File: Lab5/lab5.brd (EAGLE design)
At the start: 130 x 130 mm, 54 parts, among them J1 ISP, Q1 SI2302CDS, Q2 SI2302CDS, Q3 SI2302CDS, Q4 SI2302CDS, U1 ATMEGA128RFA1, Y1 16MHz

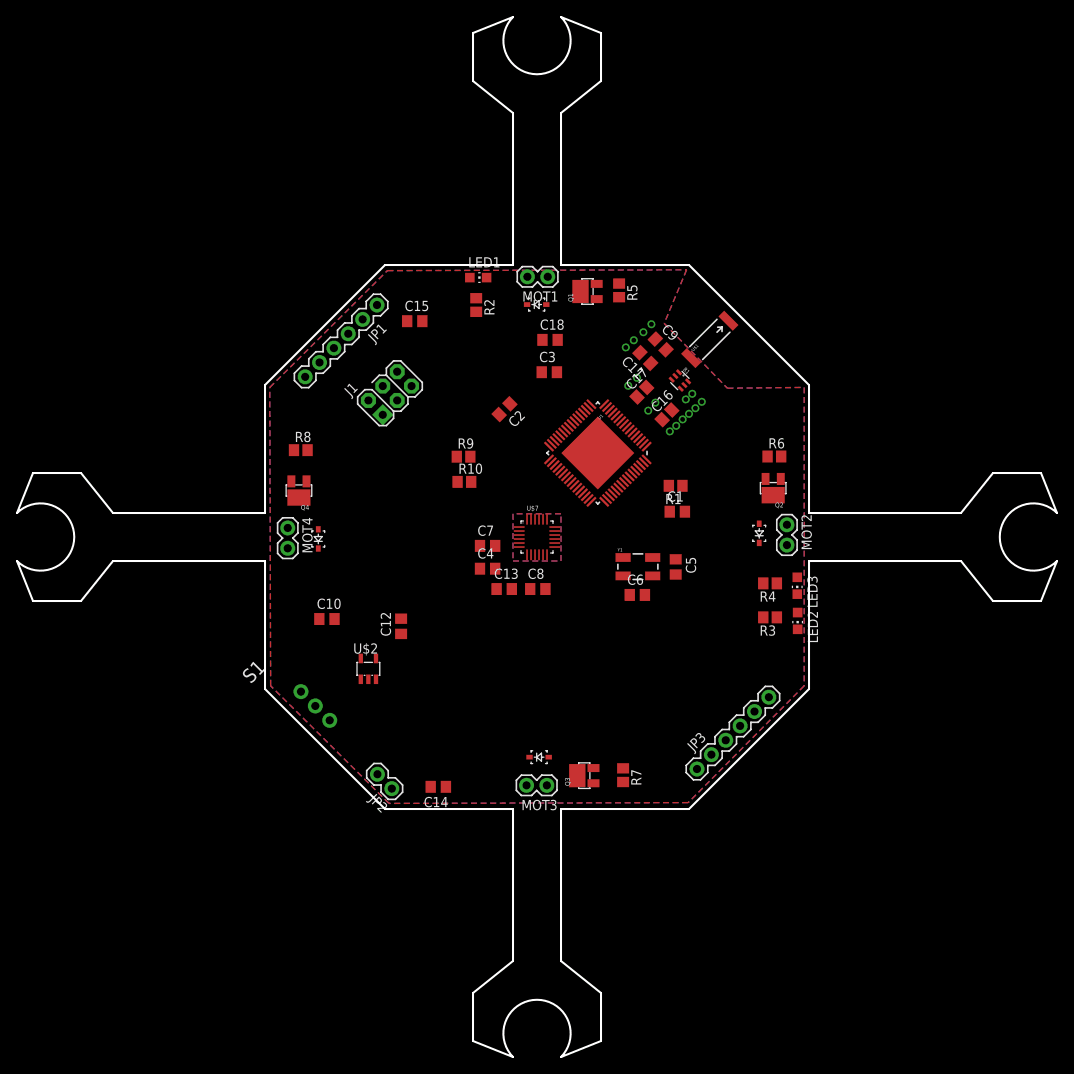
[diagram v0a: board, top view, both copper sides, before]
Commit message: working on making the board smaller
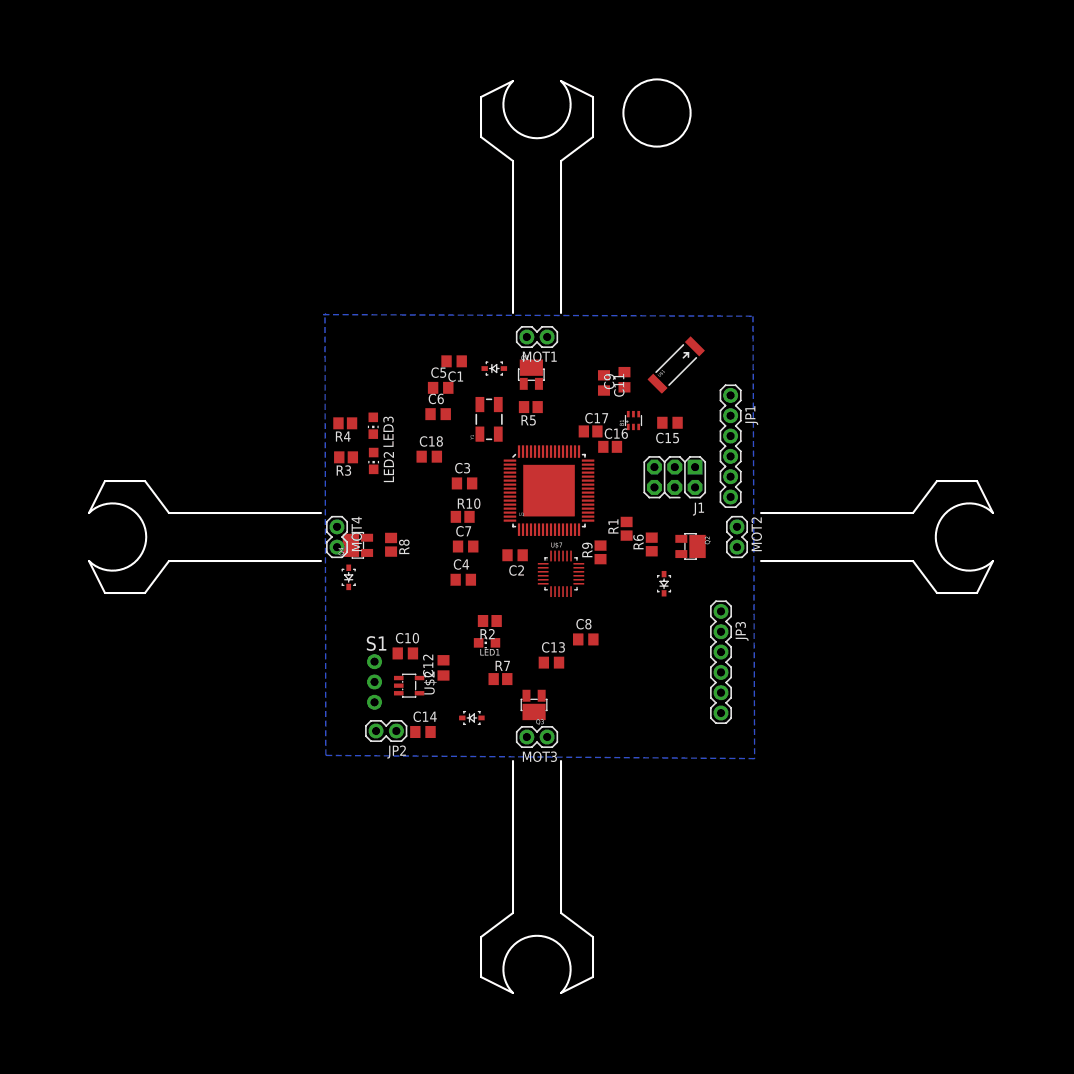
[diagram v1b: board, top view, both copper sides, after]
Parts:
- moved R4 56.7 mm to (-24.0, 14.2)
- moved LED2 56.6 mm to (-20.4, 9.51)
- moved LED3 56.6 mm to (-20.5, 13.9)
- moved R3 56.6 mm to (-23.9, 9.96)
- moved LED1 45.7 mm to (-6.25, -13.2), turned to 90 degrees
- moved JP1 45.6 mm to (24.2, 17.7), turned to 270 degrees
- moved R2 39.5 mm to (-5.90, -10.5), turned to 180 degrees
- moved J1 37.1 mm to (17.2, 7.47), turned to 180 degrees
- moved C5 36.9 mm to (-12.0, 18.6), turned to 0 degrees
- moved C15 34.3 mm to (16.6, 14.3), turned to 180 degrees
- moved C1 33.6 mm to (-10.4, 22.0), turned to 180 degrees
- moved C6 33.6 mm to (-12.4, 15.4)
- moved Y1 26.2 mm to (-5.99, 14.7), turned to 90 degrees
- moved C18 21.0 mm to (-13.5, 10.0)
- moved R9 20.9 mm to (7.94, -1.92), turned to 90 degrees
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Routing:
- removed copper zone on layer 1, net GND
- removed copper zone on layer 1, net N$1
- removed copper zone on layer 16, net N$1
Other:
- board size 130 x 130 mm -> 113 x 114.2 mm

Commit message: finisehd board. but need to add names
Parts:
- added U$3, U$4: (no value), lab5_comps:BEE_LOGO
- moved R4 39.6 mm to (15.6, 13.8), turned to 270 degrees
- moved R3 36.7 mm to (12.7, 13.7), turned to 270 degrees
- moved LED3 36.3 mm to (15.6, 18.3), turned to 0 degrees
- moved U$1 35.8 mm to (-18.2, 18.2), turned to 135 degrees
- moved LED2 34.2 mm to (12.6, 18.1), turned to 0 degrees
- moved C18 30.3 mm to (9.04, -10.3), turned to 270 degrees
- moved C9 28.5 mm to (-16.7, 12.4), turned to 225 degrees
- moved B1 25.3 mm to (-13.2, 13.6), turned to 315 degrees
- moved C11 24.9 mm to (-15.1, 10.8), turned to 45 degrees
- moved C5 21.2 mm to (9.16, 18.0), turned to 90 degrees
- moved C6 18.9 mm to (6.34, 17.9), turned to 90 degrees
- moved JP3 18.8 mm to (7.00, -19.2), turned to 0 degrees
- moved J1 18.5 mm to (14.7, -10.9), turned to 270 degrees
- moved C17 18.2 mm to (-11.2, 10.1), turned to 135 degrees
- moved C16 18.2 mm to (-8.97, 12.5), turned to 135 degrees
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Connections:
- net GND: no longer U1.65
- net PB5: now also Q2.G, R6.2; no longer Q1.G, R5.2
- net PE5: now also Q1.G, R5.2; no longer Q2.G, R6.2
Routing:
- net VBAT: track 0.00 -> 104.7 mm, vias 0 -> 1
- net 3V: track 0.00 -> 92.3 mm, vias 0 -> 6
- net GND: track 0.00 -> 43.7 mm, vias 0 -> 35
- net RESET: track 0.00 -> 41.0 mm, vias 0 -> 2
- net PE3: track 0.00 -> 27.8 mm, vias 0 -> 2
- net TX1: track 0.00 -> 24.7 mm, vias 0 -> 2
- net PE4: track 0.00 -> 24.5 mm, vias 0 -> 2
- net MOSI: track 0.00 -> 24.0 mm, vias 0 -> 1
- net RX1: track 0.00 -> 23.9 mm, vias 0 -> 2
- net N$5: track 0.00 -> 19.9 mm, vias 0 -> 2
- net SCK: track 0.00 -> 16.8 mm
- net MISO: track 0.00 -> 16.4 mm
- net RX0: track 0.00 -> 16.1 mm, vias 0 -> 2
- net PB5: track 0.00 -> 15.7 mm, vias 0 -> 2
- net TX0: track 0.00 -> 15.5 mm, vias 0 -> 2
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- added copper zone on layer 1, net GND
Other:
- board size 113 x 114.2 mm -> 104 x 104 mm

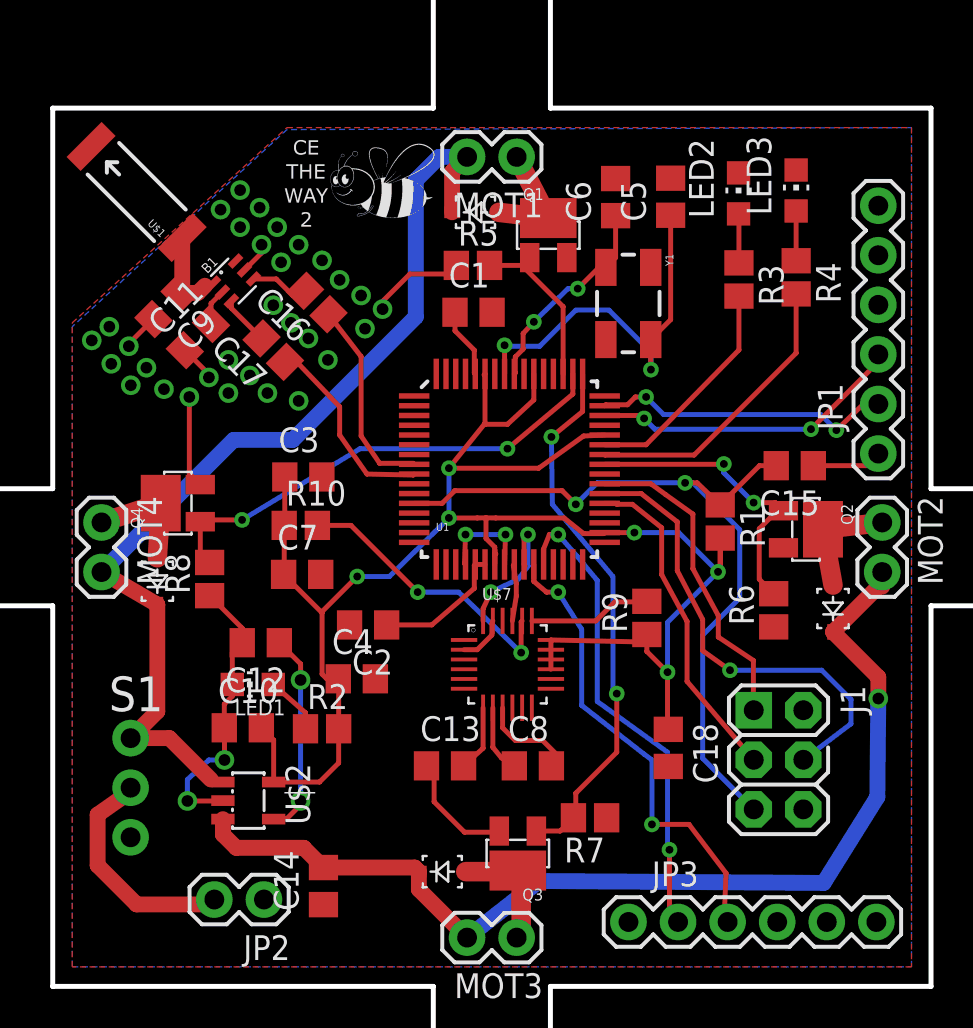
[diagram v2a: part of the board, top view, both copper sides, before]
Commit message: Update The Board Some Component Names
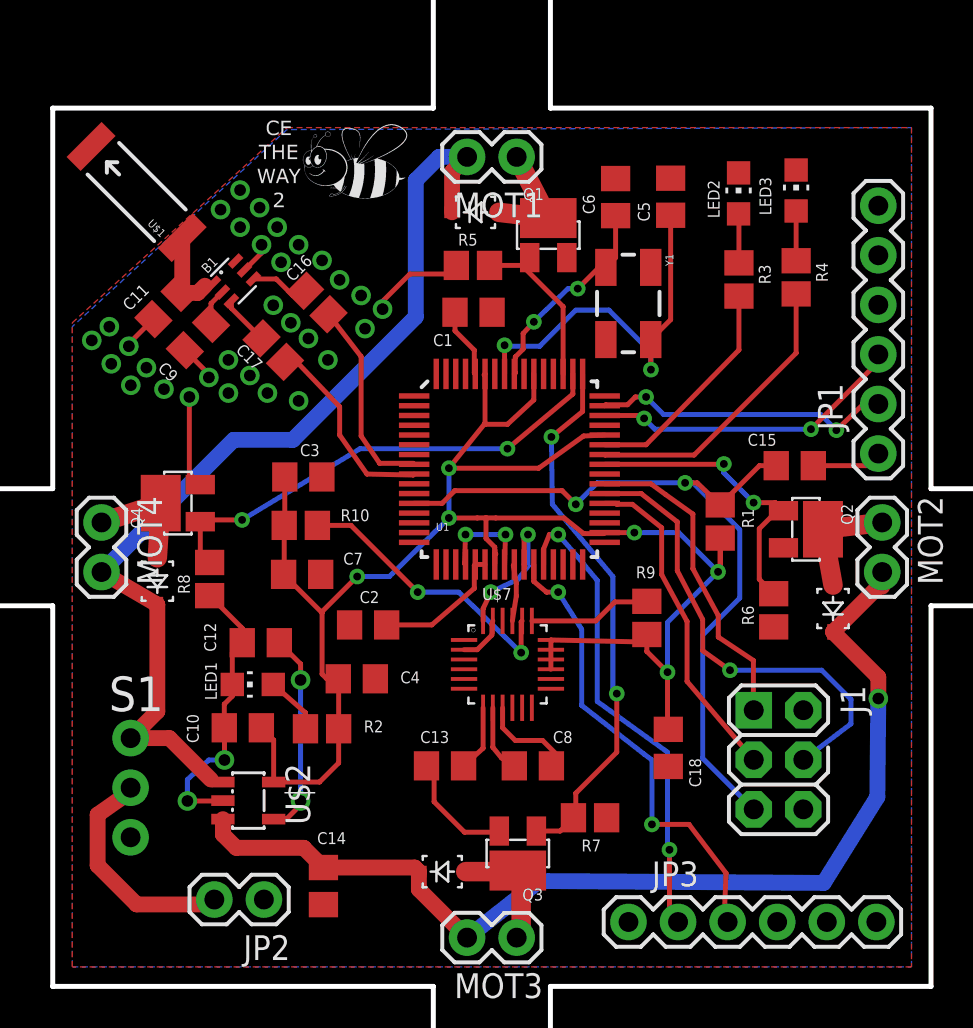
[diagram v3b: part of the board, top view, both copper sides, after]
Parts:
- moved U$3 1.72 mm to (-8.10, 19.5)

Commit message: final board design
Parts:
- moved U$3 1.04 mm to (-7.10, 19.2)
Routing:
- net GND: track 43.7 -> 33.4 mm, vias 35 -> 49
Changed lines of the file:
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@@
 <setting verticaltext="up"/>
 </settings>
-<grid distance="0.1" unitdist="mm" unit="mm" style="lines" multiple="1" display="yes" altdistance="0.025" altunitdist="inch" altunit="inch"/>
+<grid distance="0.5" unitdist="mm" unit="mm" style="lines" multiple="1" display="yes" altdistance="0.025" altunitdist="inch" altunit="inch"/>
 <layers>
 <layer number="1" name="Top" color="4" fill="1" visible="yes" active="yes"/>
@@
 <wire x1="-22.5" y1="3" x2="-22.5" y2="22.5" width="0.254" layer="20"/>
 <wire x1="-22.5" y1="-22.5" x2="-22.5" y2="-3" width="0.254" layer="20"/>
-<polygon width="0.254" layer="41">
-<vertex x="-22" y="21.9"/>
-<vertex x="-22" y="11"/>
-<vertex x="-10" y="22"/>
-<vertex x="-22" y="22"/>
-</polygon>
 <polygon width="0.254" layer="42">
 <vertex x="-22" y="22"/>
-<vertex x="-22" y="11"/>
-<vertex x="-10" y="22"/>
+<vertex x="-10.5" y="22"/>
+<vertex x="-22" y="11.5"/>
+</polygon>
+<polygon width="0.254" layer="41">
+<vertex x="-22" y="22"/>
+<vertex x="-10.5" y="22"/>
+<vertex x="-22" y="11.5"/>
 </polygon>
 </plain>
@@
 <attribute name="TOL" value="" x="-17.14" y="-1.74" size="1.778" layer="27" rot="R90" display="off"/>
 </element>
-<element name="U$3" library="lab5_comps" package="BEE_LOGO" value="" x="-8.1" y="19.5"/>
+<element name="U$3" library="lab5_comps" package="BEE_LOGO" value="" x="-7.1" y="19.2"/>
 <element name="U1" library="lab5_comps" package="QFN-64" value="ATMEGA128RFA1" x="0.9" y="4"/>
 <element name="U$4" library="lab5_comps" package="BEE_LOGO" value="" x="0.3" y="32.8" rot="R90"/>
@@
 <wire x1="-14.46" y1="-2.48" x2="-12.79" y2="-4.15" width="0.254" layer="1"/>
 <wire x1="-12.79" y1="-4.15" x2="-12.79" y2="-4.89" width="0.254" layer="1"/>
-<wire x1="-13.71" y1="-8.04" x2="-13.71" y2="-9.25" width="0.254" layer="1"/>
 <wire x1="-13.71" y1="-9.25" x2="-13.7" y2="-9.25" width="0.254" layer="1"/>
-<wire x1="-13.7" y1="-9.25" x2="-13.7" y2="-10.9" width="0.254" layer="1"/>
-<via x="-13.7" y="-10.9" extent="1-16" drill="0.6"/>
-<wire x1="-13.7" y1="-10.9" x2="-14.5" y2="-10.9" width="0.254" layer="16"/>
-<wire x1="-14.5" y1="-10.9" x2="-15.6" y2="-11.9" width="0.254" layer="16"/>
-<wire x1="-15.6" y1="-11.9" x2="-15.6" y2="-13" width="0.254" layer="16"/>
-<via x="-15.6" y="-13" extent="1-16" drill="0.6"/>
-<wire x1="-15.6" y1="-13" x2="-13.8" y2="-13" width="0.254" layer="1"/>
-<wire x1="-13.8" y1="-13" x2="-13.78" y2="-12.98" width="0.254" layer="1"/>
-<wire x1="-13.71" y1="-8.04" x2="-13.3" y2="-7.63" width="0.254" layer="1"/>
 <wire x1="-13.3" y1="-7.63" x2="-13.3" y2="-7.03" width="0.254" layer="1"/>
 <wire x1="-12.79" y1="-4.89" x2="-13.3" y2="-5.4" width="0.254" layer="1"/>
-<wire x1="-13.3" y1="-5.4" x2="-13.3" y2="-7.03" width="0.254" layer="1"/>
 <wire x1="-3.35" y1="-11.2" x2="-2.96" y2="-11.2" width="0.254" layer="1"/>
 <wire x1="-15.5" y1="7.7" x2="-15.5" y2="3.77" width="0.254" layer="1"/>
@@
 <wire x1="-1.4" y1="-14.6" x2="0.32" y2="-14.6" width="0.254" layer="1"/>
 <wire x1="0.32" y1="-14.6" x2="0.38" y2="-14.54" width="0.254" layer="1"/>
+<via x="-7.2" y="-12.5" extent="1-16" drill="0.4"/>
+<via x="-6.2" y="-14" extent="1-16" drill="0.4"/>
+<via x="-4.4" y="-14.1" extent="1-16" drill="0.4"/>
+<via x="-2.5" y="-14.1" extent="1-16" drill="0.4"/>
+<via x="-5.8" y="-11.2" extent="1-16" drill="0.4"/>
+<via x="-4.6" y="-9.2" extent="1-16" drill="0.4"/>
+<via x="-20.4" y="7" extent="1-16" drill="0.4"/>
+<via x="-19.6" y="4.7" extent="1-16" drill="0.4"/>
+<via x="-17.1" y="5.2" extent="1-16" drill="0.4"/>
+<via x="-18.3" y="6.5" extent="1-16" drill="0.4"/>
+<via x="-6.1" y="14.7" extent="1-16" drill="0.4"/>
+<via x="-7.4" y="15.8" extent="1-16" drill="0.4"/>
+<via x="10.5" y="10.6" extent="1-16" drill="0.4"/>
+<via x="10.6" y="13.3" extent="1-16" drill="0.4"/>
+<via x="-5.9" y="-19.9" extent="1-16" drill="0.4"/>
+<via x="-17.5" y="-20.5" extent="1-16" drill="0.4"/>
 <wire x1="5.781" y1="6.25" x2="5.781" y2="1.25" width="0" layer="19" extent="1-1"/>
 <wire x1="1.65" y1="8.881" x2="5.781" y2="6.25" width="0" layer="19" extent="1-1"/>
@@
 </signal>
 </signals>
+<errors>
+</errors>
 </board>
 </drawing>

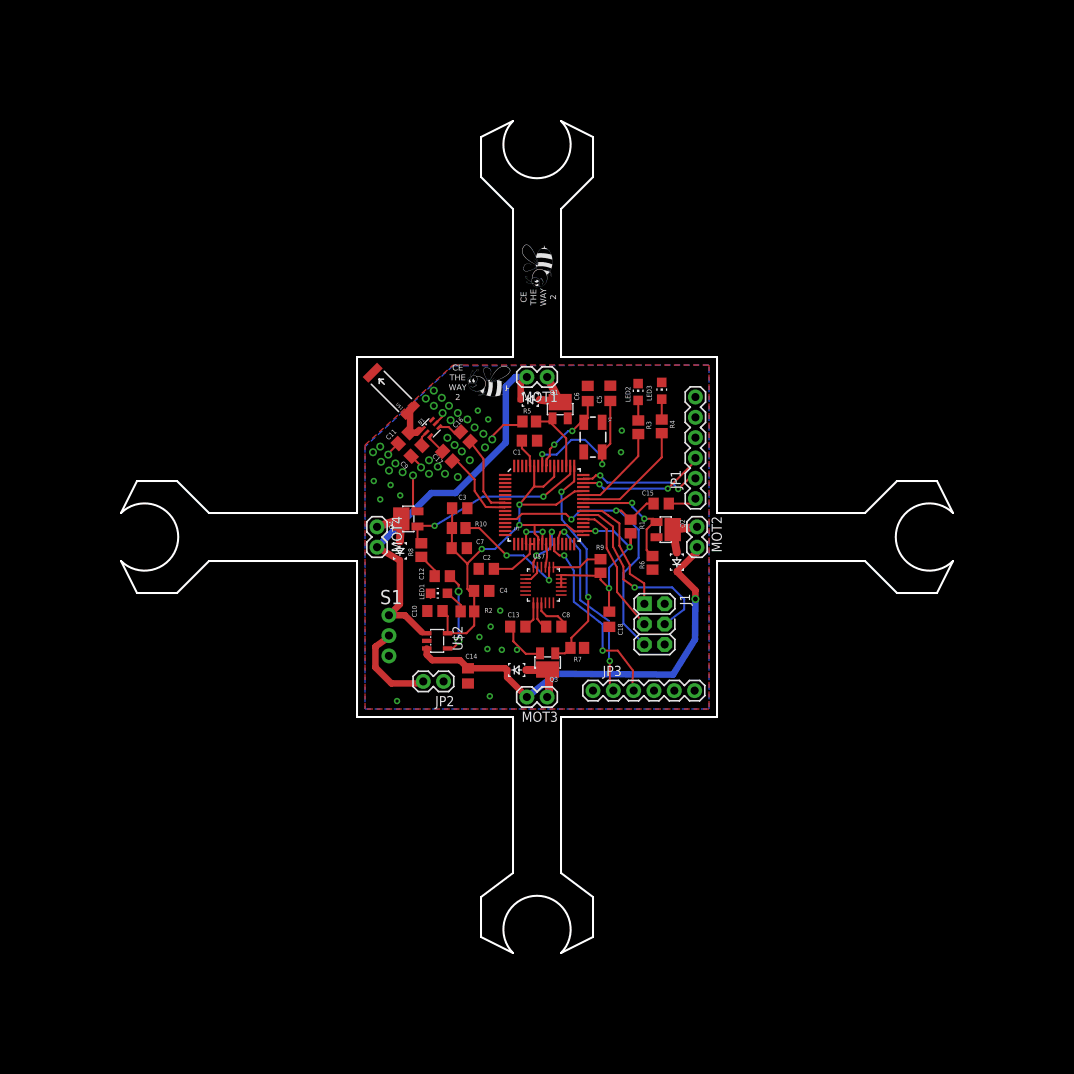
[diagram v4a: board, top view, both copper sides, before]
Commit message: fixed imu gnd plane
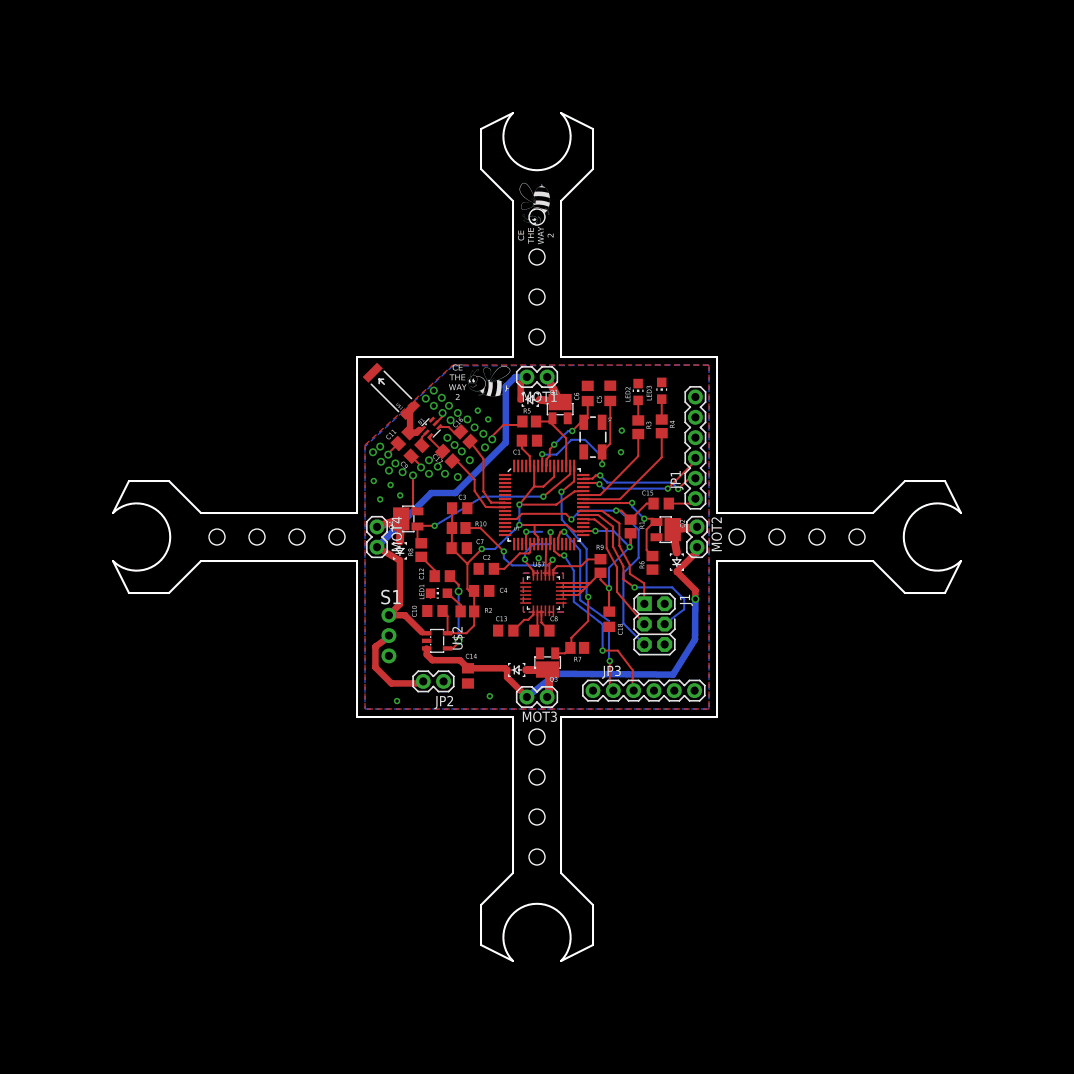
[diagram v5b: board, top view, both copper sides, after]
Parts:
- moved U$4 7.71 mm to (0.00, 40.5)
- moved C13 1.58 mm to (-3.90, -11.7)
- moved C8 1.58 mm to (0.60, -11.7)
- moved U$7 1.00 mm to (0.80, -7.00)
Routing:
- net GND: track 33.4 -> 23.2 mm, vias 49 -> 43
- net 3V: track 92.3 -> 101.2 mm
- net SDA: track 7.33 -> 9.81 mm
- net N$26: track 5.12 -> 2.89 mm
- net SCL: track 2.94 -> 3.90 mm
- net N$30: track 14.8 -> 15.7 mm
- net N$25: track 3.51 -> 2.64 mm
- net N$29: track 6.31 -> 7.12 mm
- added copper zone on layer 1, net N$13
- added copper zone on layer 16, net N$13
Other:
- board size 104 x 104 mm -> 106 x 106 mm
